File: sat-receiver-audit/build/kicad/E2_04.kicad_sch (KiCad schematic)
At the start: 54 parts, among them U214 TPS259630DDAR, U215 INA3221AIRGVR, U216 INA3221AIRGVR, U217 TLV3011BIDBVR, U218 TLV3011BIDBVR, U219 TLV3011BIDBVR, U220 TPS3701DDCR

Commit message: SR-RX-v2.1: review fixes on the Codex branch, readable schematic, one-file bundle
Independent review of the Codex branch (schematic vs STACK.md, hard rules,
security, tests) found no blockers; this commit applies its findings:

- rules in code: Cospas-Sarsat 406.0-406.1 MHz added to the no-data mask;
  Q6A Wi-Fi/BT off in the field/QUIET root (modprobe blacklist, udev
  authorized=0 on FE1.1s port 4, rfkill) with self-checks; device denylist
  completed per STACK (gr-gsm, gr-iridium, kalibrate, pager/trunking decoders,
  TX-capable tools); W1-2 WIFI_PWR_EN as blocking open item E5-10
- STACK.md is the source of truth again; v2.1 changes recorded in it; the
  "historical" marker kept only on ISDT/raw-balance rows; gender-neutral wording
- schematic data: open values shown as TBD with start values and notes, U503
  TPS2553DBVR-1, Lime X2/X4 RX mapping TBD, 37 open items drawn on the sheets
- schematic readability: wired groups, junctions, GND symbols, standard
  transistor/diode symbols; netlist unchanged (603 nets identical)
- tooling: reproducible run_checks (no timestamps or machine paths), pinned
  dependencies, bundle excludes cache folders, clean-checkout bundle check
- regenerated: KiCad export (14 pages), netlist/ERC, module lab, PCB inputs,
  readiness contract, acceptance hashes, SR-RX-v2-ves-proekt.html

Checks: ERC 0 errors/0 warnings, netlist comparison PASS, 432 tests (431
passed, 1 skipped), deployment tests OK, bundle check PASS on a clean checkout.

History note: earlier versions of the generated SR-RX-v2-ves-proekt.html and
handoff/handoff-bundle.zip were removed from history; only the final versions
are kept. The Codex merge commit is now attributed to Codex.

Co-Authored-By: Claude Opus 5.5 <noreply@anthropic.com>
Claude-Session: https://claude.ai/code/session_01W9CKpimWpgkUmrDQQMiKtF
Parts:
- removed C269: 100nF 50V X7R C1608X7R1H104K080AA, Capacitor_SMD:C_0603_1608Metric, symbol sr_rx_v2_completed:C_C269
- removed C270: 1uF 50V X7R C2012X7R1H105K125AB, Capacitor_SMD:C_0805_2012Metric, symbol sr_rx_v2_completed:C_C270
- removed C271: 1uF 50V X7R C2012X7R1H105K125AB, Capacitor_SMD:C_0805_2012Metric, symbol sr_rx_v2_completed:C_C271
- removed C272: 1uF 50V X7R C2012X7R1H105K125AB, Capacitor_SMD:C_0805_2012Metric, symbol sr_rx_v2_completed:C_C272
- removed C273: 47uF 50V EEUFR1H470, symbol sr_rx_v2_completed:C_C273
- removed C282: 10nF 50V C0G C1608C0G1H103J080AA, Capacitor_SMD:C_0603_1608Metric, symbol sr_rx_v2_completed:C_C282
- removed C283: 100nF 50V X7R C1608X7R1H104K080AA, Capacitor_SMD:C_0603_1608Metric, symbol sr_rx_v2_completed:C_C283
- removed C284: 10nF 50V C0G C1608C0G1H103J080AA, Capacitor_SMD:C_0603_1608Metric, symbol sr_rx_v2_completed:C_C284
- removed C285: 100nF 50V X7R C1608X7R1H104K080AA, Capacitor_SMD:C_0603_1608Metric, symbol sr_rx_v2_completed:C_C285
- removed C286: 10nF 50V C0G C1608C0G1H103J080AA, Capacitor_SMD:C_0603_1608Metric, symbol sr_rx_v2_completed:C_C286
- removed C287: 100nF 50V X7R C1608X7R1H104K080AA, Capacitor_SMD:C_0603_1608Metric, symbol sr_rx_v2_completed:C_C287
- removed C294: 22uF 50V X7R C3225X7R1H226M250AC, Capacitor_SMD:C_1210_3225Metric, symbol sr_rx_v2_completed:C_C294
- removed D203: PMEG4030ER, Diode_SMD:Nexperia_CFP3_SOD-123W, symbol sr_rx_v2_completed:C_D203
- removed L214: 1uH XAL5030-102MEC, symbol sr_rx_v2_completed:C_L214
- removed R262: 7.87k 1%, symbol sr_rx_v2_completed:C_R262
- removed R263: 112k 0.1%, symbol sr_rx_v2_completed:C_R263
- removed R264: 10.0k 0.1%, symbol sr_rx_v2_completed:C_R264
- removed R266: 0.200R 0.1% 0.25W Kelvin, symbol sr_rx_v2_completed:C_R266
- removed R267: 0.22R 1% 0.25W, symbol sr_rx_v2_completed:C_R267
- removed R280: 85.6k 0.1%, symbol sr_rx_v2_completed:C_R280
- removed R281: 10.0k 0.1%, symbol sr_rx_v2_completed:C_R281
- removed R283: 90.9k 0.1%, symbol sr_rx_v2_completed:C_R283
- removed R284: 10.0k 0.1%, symbol sr_rx_v2_completed:C_R284
- removed R286: 73.2k 0.1%, symbol sr_rx_v2_completed:C_R286
- removed R287: 10.0k 0.1%, symbol sr_rx_v2_completed:C_R287
- removed R288: TNPW0805332KBYEA 332k 0.1%10ppm, symbol sr_rx_v2_completed:C_R288
- removed TP212: BONI13V8, symbol sr_rx_v2_completed:C_TP212
- removed U214: TPS259630DDAR, symbol sr_rx_v2_completed:C_U214
- removed U217: TLV3011BIDBVR, symbol sr_rx_v2_completed:C_U217
- removed U218: TLV3011BIDBVR, symbol sr_rx_v2_completed:C_U218
- removed U219: TLV3011BIDBVR, symbol sr_rx_v2_completed:C_U219
- removed U220: TPS3701DDCR, symbol sr_rx_v2_completed:C_U220
- added C295: 1uF 50V X7R C2012X7R1H105K125AB, Capacitor_SMD:C_0805_2012Metric, symbol sr_rx_v2_completed:C_C295
- added C296: 1uF 50V X7R C2012X7R1H105K125AB, Capacitor_SMD:C_0805_2012Metric, symbol sr_rx_v2_completed:C_C296
- added C297: 1uF 50V X7R C2012X7R1H105K125AB, Capacitor_SMD:C_0805_2012Metric, symbol sr_rx_v2_completed:C_C297
- added C298: 47uF 50V EEUFR1H470, symbol sr_rx_v2_completed:C_C298
- added L215: 1uH XAL5030-102MEC, symbol sr_rx_v2_completed:C_L215
- added R293: 162k 1%, symbol sr_rx_v2_completed:C_R293
- added R294: 100k 1%, symbol sr_rx_v2_completed:C_R294
- added R295: 0.22R 1%0.25W, symbol sr_rx_v2_completed:C_R295
- added TP216: BIAS_SB_LNA, symbol sr_rx_v2_completed:C_TP216
- added U221: TPS2553DBVR-1, symbol sr_rx_v2_completed:C_U221
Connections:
- net GND: now also C295.2, C296.2, C297.2, C298.2 (-), R293.2, R294.2, U221.2 (GND)
- new net BIAS_SB_LNA: C297.1, L215.2, R295.1, TP216.1 (TP)
- new net E2_SB_DAMP: C298.1 (+), R295.2
- new net E2_SB_ILIM: R293.1, U221.5 (ILIM)
- new net E2_SB_SW: C296.1, L215.1, U221.6 (OUT)
- new net EN_SB_LNA: R294.1, U221.3 (EN)
- new net FLT_SB_LNA: U221.4 (FAULT)
- new net LAB5: C295.1, U221.1 (IN)
- no-connect marks 9 -> 8
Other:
- note added: "E2 - Захищені рейки, LNA і моніторинг струму (4/4)"
- note added: "S-band LaNA WB: захищена шина 5 V"
- note added: "Дроти з'єднують контакти всередині функціональної групи; кожне дерево дротів має одну глобальну мітку з канонічною назвою мережі (рамка-стрілка — мережа виходить за межі групи, пряма рамка — мережа лише цієї групи). Однакові мітки з'єднані на всіх аркушах; земля — символ GND. Рамки OPEN — незакриті ворота з design/E#.json (повний реєстр: OPEN_ITEMS.md); «TBD» у значенні — STACK номіналу не задає,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"
- note removed: "AUX12: контроль напруги після PTC"
- note removed: "Boni: контроль напруги"
- note removed: "Boni: малошумна захищена шина"
- note removed: "E2 - Захищені рейки, LNA і моніторинг струму (4/5)"
- note removed: "LNB: контроль напруги"
- note removed: "LNB: незалежне точне відсікання OVP"
- note removed: "Мережі з однаковими глобальними мітками електрично з'єднані на всіх аркушах. Фізичні/функціональні контакти: див. design/ і OPEN_ITEMS.md."
- title: E2 - Захищені рейки, LNA і моніторинг струму (4/5) -> E2 - Захищені рейки, LNA і моніторинг струму (4/4)
- moved on the sheet: U215, U216

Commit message: Stage 2 integration: CAD and DC_CORE re-freeze from CI run 40094234222; bound-count test and PCB hash lists follow
Co-Authored-By: Claude Opus 5.5 <noreply@anthropic.com>
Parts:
- removed C274: 100nF 50V X7R C1608X7R1H104K080AA, Capacitor_SMD:C_0603_1608Metric, symbol sr_rx_v2_completed:C_C274
- removed C275: 100nF 50V X7R C1608X7R1H104K080AA, Capacitor_SMD:C_0603_1608Metric, symbol sr_rx_v2_completed:C_C275
- removed C276: 100nF 50V X7R C1608X7R1H104K080AA, Capacitor_SMD:C_0603_1608Metric, symbol sr_rx_v2_completed:C_C276
- removed C277: 100nF 50V X7R C1608X7R1H104K080AA, Capacitor_SMD:C_0603_1608Metric, symbol sr_rx_v2_completed:C_C277
- removed C278: 100nF 50V X7R C1608X7R1H104K080AA, Capacitor_SMD:C_0603_1608Metric, symbol sr_rx_v2_completed:C_C278
- removed C279: 100nF 50V X7R C1608X7R1H104K080AA, Capacitor_SMD:C_0603_1608Metric, symbol sr_rx_v2_completed:C_C279
- removed C280: 100nF 50V X7R C1608X7R1H104K080AA, Capacitor_SMD:C_0603_1608Metric, symbol sr_rx_v2_completed:C_C280
- removed C281: 100nF 50V X7R C1608X7R1H104K080AA, Capacitor_SMD:C_0603_1608Metric, symbol sr_rx_v2_completed:C_C281
- removed C295: 1uF 50V X7R C2012X7R1H105K125AB, Capacitor_SMD:C_0805_2012Metric, symbol sr_rx_v2_completed:C_C295
- removed C296: 1uF 50V X7R C2012X7R1H105K125AB, Capacitor_SMD:C_0805_2012Metric, symbol sr_rx_v2_completed:C_C296
- removed C297: 1uF 50V X7R C2012X7R1H105K125AB, Capacitor_SMD:C_0805_2012Metric, symbol sr_rx_v2_completed:C_C297
- removed C298: 47uF 50V EEUFR1H470, symbol sr_rx_v2_completed:C_C298
- removed L215: 1uH XAL5030-102MEC, symbol sr_rx_v2_completed:C_L215
- removed R268: 10.0R 1%, symbol sr_rx_v2_completed:C_R268
- removed R269: 10.0R 1%, symbol sr_rx_v2_completed:C_R269
- removed R270: 10.0R 1%, symbol sr_rx_v2_completed:C_R270
- removed R271: 10.0R 1%, symbol sr_rx_v2_completed:C_R271
- removed R272: 10.0R 1%, symbol sr_rx_v2_completed:C_R272
- removed R273: 10.0R 1%, symbol sr_rx_v2_completed:C_R273
- removed R274: 10.0R 1%, symbol sr_rx_v2_completed:C_R274
- removed R275: 10.0R 1%, symbol sr_rx_v2_completed:C_R275
- removed R276: 10.0R 1%, symbol sr_rx_v2_completed:C_R276
- removed R277: 10.0R 1%, symbol sr_rx_v2_completed:C_R277
- removed R278: 10.0R 1%, symbol sr_rx_v2_completed:C_R278
- removed R279: 10.0R 1%, symbol sr_rx_v2_completed:C_R279
- removed R293: 162k 1%, symbol sr_rx_v2_completed:C_R293
- removed R294: 100k 1%, symbol sr_rx_v2_completed:C_R294
- removed R295: 0.22R 1%0.25W, symbol sr_rx_v2_completed:C_R295
- removed TP216: BIAS_SB_LNA, symbol sr_rx_v2_completed:C_TP216
- removed U215: INA3221AIRGVR, symbol sr_rx_v2_completed:C_U215
- removed U216: INA3221AIRGVR, symbol sr_rx_v2_completed:C_U216
- removed U221: TPS2553DBVR-1, symbol sr_rx_v2_completed:C_U221
- added C252: 10uF 50V X7R C3225X7R1H106K250AC, Capacitor_SMD:C_1210_3225Metric, symbol sr_rx_v2_completed:C_C252
- added C253: 10uF 50V X7R C3225X7R1H106K250AC, Capacitor_SMD:C_1210_3225Metric, symbol sr_rx_v2_completed:C_C253
- added C254: 47uF 50V EEUFR1H470, symbol sr_rx_v2_completed:C_C254
- added C255: 10uF 50V X7R C3225X7R1H106K250AC, Capacitor_SMD:C_1210_3225Metric, symbol sr_rx_v2_completed:C_C255
- added C256: 22uF 50V X7R C3225X7R1H226M250AC, Capacitor_SMD:C_1210_3225Metric, symbol sr_rx_v2_completed:C_C256
- added C257: 1uF 50V X7R C2012X7R1H105K125AB, Capacitor_SMD:C_0805_2012Metric, symbol sr_rx_v2_completed:C_C257
- added C258: 47nF 50V X7R C1608X7R1H473K080AA, Capacitor_SMD:C_0603_1608Metric, symbol sr_rx_v2_completed:C_C258
- added C259: 1uF 50V X7R C2012X7R1H105K125AB, Capacitor_SMD:C_0805_2012Metric, symbol sr_rx_v2_completed:C_C259
- added C260: 1uF 50V X7R C2012X7R1H105K125AB, Capacitor_SMD:C_0805_2012Metric, symbol sr_rx_v2_completed:C_C260
- added C261: 1uF 50V X7R C2012X7R1H105K125AB, Capacitor_SMD:C_0805_2012Metric, symbol sr_rx_v2_completed:C_C261
- added C262: 47uF 50V EEUFR1H470, symbol sr_rx_v2_completed:C_C262
- added C293: 22uF 50V X7R C3225X7R1H226M250AC, Capacitor_SMD:C_1210_3225Metric, symbol sr_rx_v2_completed:C_C293
- added D202: PMEG4030ER, Diode_SMD:Nexperia_CFP3_SOD-123W, symbol sr_rx_v2_completed:C_D202
- added L211: 1uH XAL5030-102MEC, symbol sr_rx_v2_completed:C_L211
- added L212: 1uH XAL5030-102MEC, symbol sr_rx_v2_completed:C_L212
- added R252: 0.22R 1% 0.25W, symbol sr_rx_v2_completed:C_R252
- added R253: 100k 1%, symbol sr_rx_v2_completed:C_R253
- added R254: 2.05k 1%, symbol sr_rx_v2_completed:C_R254
- added R255: 110k 0.5%, symbol sr_rx_v2_completed:C_R255
- added R256: 10.0k 0.5%, symbol sr_rx_v2_completed:C_R256
- added R258: 0.100R 0.1% 0.25W Kelvin, symbol sr_rx_v2_completed:C_R258
- added R259: 0.22R 1% 0.25W, symbol sr_rx_v2_completed:C_R259
- added TP211: LNB13V2, symbol sr_rx_v2_completed:C_TP211
- added U211: TPS7A4701RGWT, symbol sr_rx_v2_completed:C_U211
- added U212: TPS259630DDAR, symbol sr_rx_v2_completed:C_U212
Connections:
- net E2_LNB_EF: now also C259.1, R258.1, U212.5 (OUT)
- net E2_LNB_MON: now also C260.1, L212.1, R258.2
- net GND: now also C252.2, C253.2, C254.2 (-), C255.2, C256.2, C257.2, C258.2, C259.2, C260.2, C261.2, C262.2 (-), C293.2, D202.2 (A), R253.2, R254.2, R256.2, U211.10 (0P4V), U211.11 (0P2V), U211.5 (6P4V1), U211.6 (3P2V), U211.7 (GND), U211.8 (1P6V), U211.EP, U212.1 (GND), U212.EP
- new net E1_SW: C252.1, L211.1
- new net E2_LNB_DVDT: C258.1, U212.2 (dVdt)
- new net E2_LNB_ILM: R254.1, U212.7 (ILM)
- new net E2_LNB_IN: C253.1, C255.1, L211.2, R252.1, U211.15 (IN), U211.16 (IN)
- new net E2_LNB_IN_DAMP: C254.1 (+), R252.2
- new net E2_LNB_LDO: C256.1, C293.1, D202.1 (K), R255.1, U211.1 (OUT), U211.20 (OUT), U211.3 (SENSE/FB), U212.4 (IN)
- new net E2_LNB_NR: C257.1, U211.14 (NR)
- new net E2_LNB_OV: R255.2, R256.1, U212.8 (OVLO)
- new net EN_LNB: R253.1, U211.13 (EN)
- new net FLT_LNB: U212.6 (FLT)
- new net LNB13V2: C261.1, L212.2, R259.1, TP211.1 (TP)
- new net LNB13V2_DAMP: C262.1 (+), R259.2
- new net OVP_LNB_N: U212.3 (EN/UVLO)
- no-connect marks 8 -> 7
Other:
- note added: "E2 - Захищені рейки, LNA і моніторинг струму (4/5)"
- note added: "E2-02 — OPEN, блокує випуск — STACK §5.1 (LNB13V2); §8 (TPS7A4701); §8.1 RF-4"
- note added: "LNB: малошумна захищена шина"
- note added: "Позначення фізичних джерел живлення (ERC)"
- note added: "Статичне вікно OVP LNB закрито TPS3701: 13.56–13.96V. Швидкий викид при відмові LDO не обмежено гарантованим максимальним часом у даташитах: 9.9µs компаратора і близько 12µs EN-off eFuse задані лише типово. Ворота (стенд): Без LNB і зі струмовим обмеженням подати на вузол LDO контрольований стрибок 13.2→16.4V; осцилографувати F-вихід при мін./макс. навантаженні, на холоді й при 50°C. Отримати гра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"
- note removed: "E2 - Захищені рейки, LNA і моніторинг струму (4/4)"
- note removed: "INA3221: струми LNA1–3"
- note removed: "INA3221: струми LNA4, LNB і Boni"
- note removed: "S-band LaNA WB: захищена шина 5 V"
- title: E2 - Захищені рейки, LNA і моніторинг струму (4/4) -> E2 - Захищені рейки, LNA і моніторинг струму (4/5)

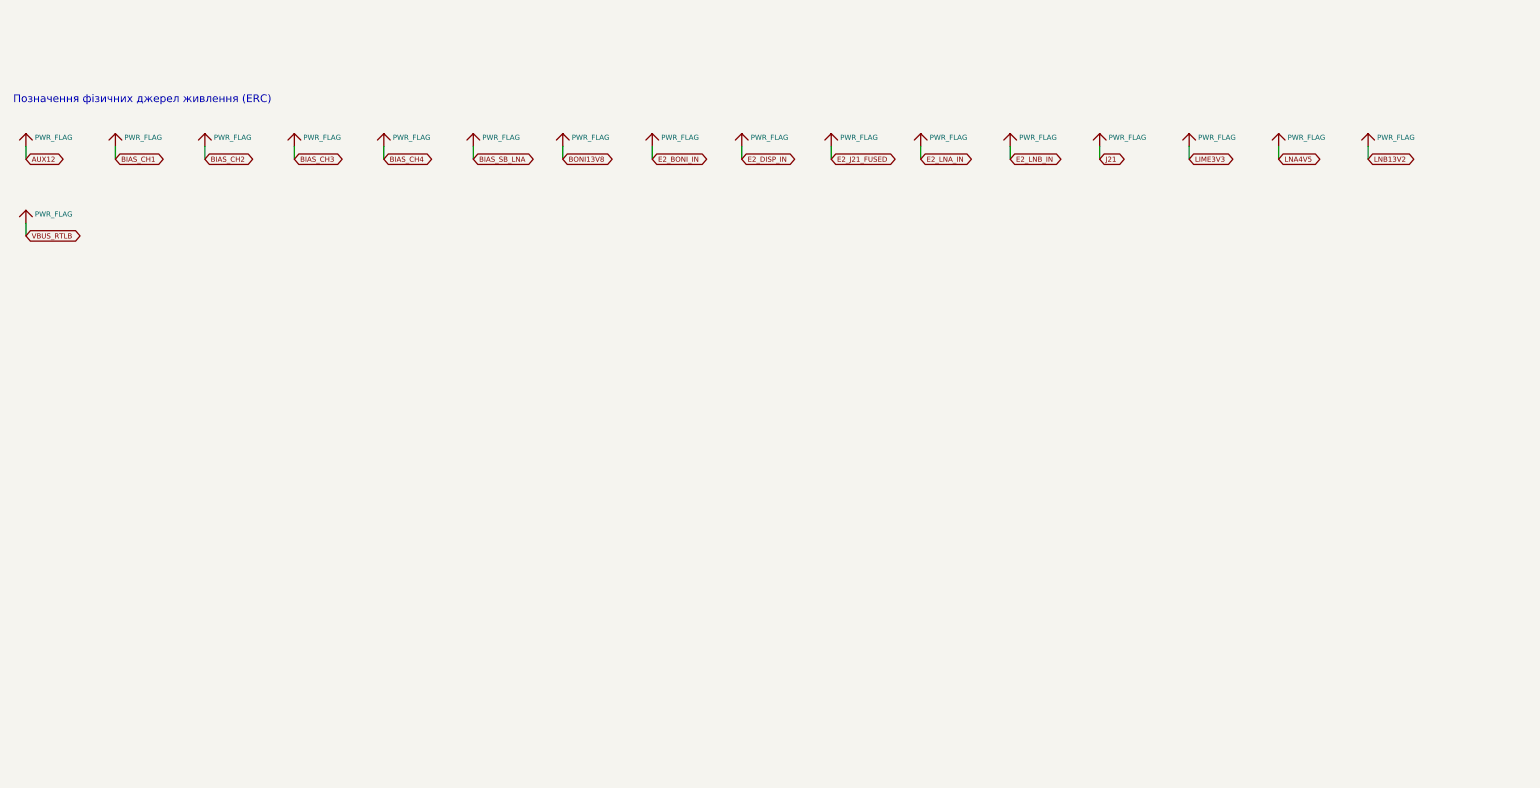
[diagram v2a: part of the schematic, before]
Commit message: GENERATED: CAD, documents, verification reports, DC_CORE re-freeze and module-lab inventory for f3f57e8
Applied unchanged from the cad-regenerated artifact of CI run 40109759054
(workflow_dispatch, refreeze_pcb=true, KiCad 10.0.7): schematics, SVG, PDF,
netlist, OPEN_ITEMS.md, COMPLETION.md, verification/{electrical-invariants,
independent-netlist-review,netlist,pcb-review,pcb-prototype-review,
pdf-export,validation}, pcb/generated and the re-frozen DC_CORE starter and
routed prototype with their pinned hashes. Inputs: the stage 3A merge,
design/E2.json (PICO-2 text) and STACK.md (2.7 row).

deployment/module_lab/inventory.json: source_snapshots only, from
deployment/module_lab/refresh_inventory.py (E2.json and STACK.md bytes).

Co-Authored-By: Claude Opus 5.5 <noreply@anthropic.com>
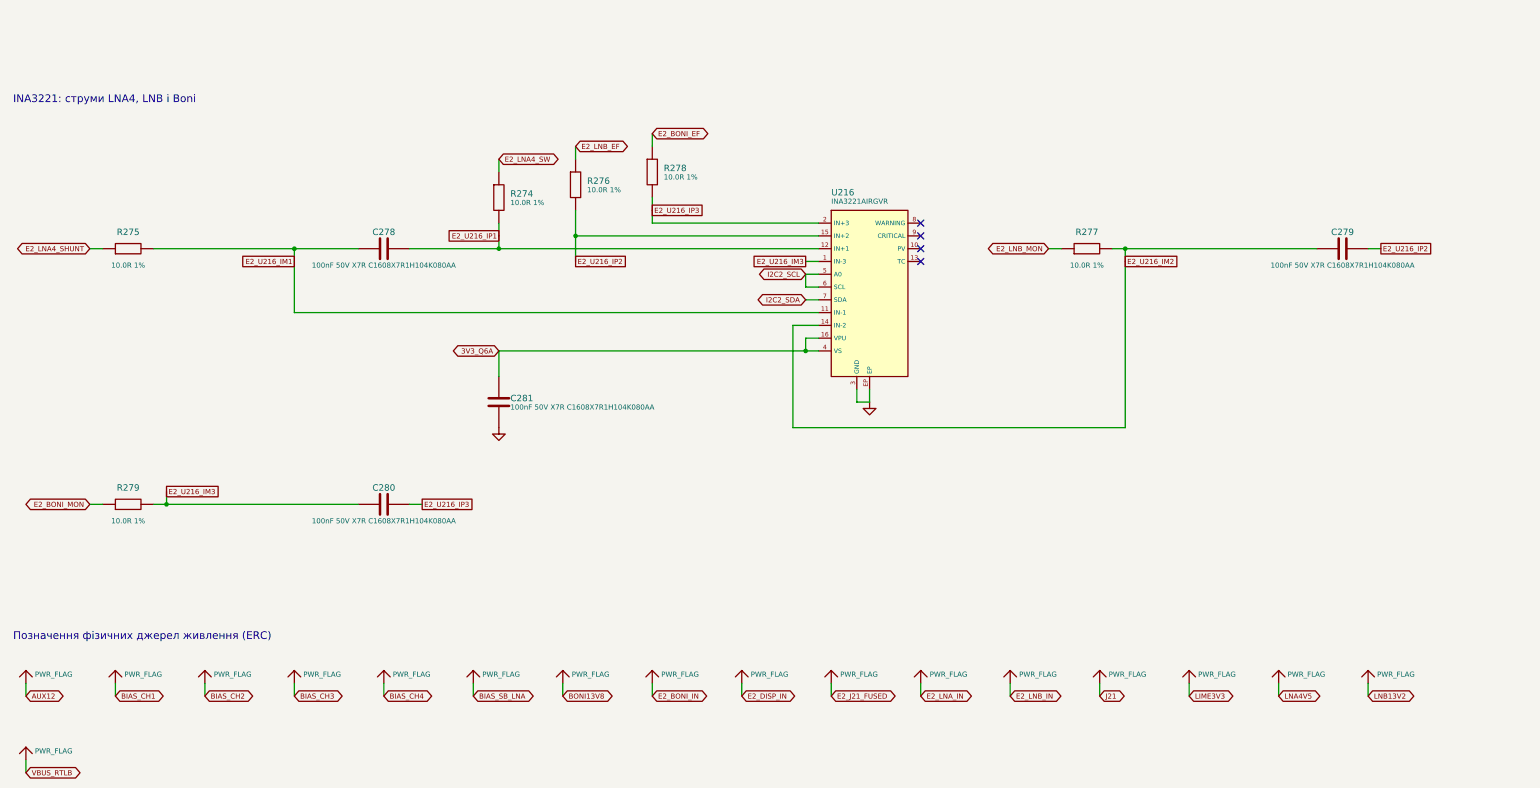
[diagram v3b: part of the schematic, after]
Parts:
- added C278: 100nF 50V X7R C1608X7R1H104K080AA, Capacitor_SMD:C_0603_1608Metric, symbol sr_rx_v2_completed:C_C278
- added C279: 100nF 50V X7R C1608X7R1H104K080AA, Capacitor_SMD:C_0603_1608Metric, symbol sr_rx_v2_completed:C_C279
- added C280: 100nF 50V X7R C1608X7R1H104K080AA, Capacitor_SMD:C_0603_1608Metric, symbol sr_rx_v2_completed:C_C280
- added C281: 100nF 50V X7R C1608X7R1H104K080AA, Capacitor_SMD:C_0603_1608Metric, symbol sr_rx_v2_completed:C_C281
- added R274: 10.0R 1%, symbol sr_rx_v2_completed:C_R274
- added R275: 10.0R 1%, symbol sr_rx_v2_completed:C_R275
- added R276: 10.0R 1%, symbol sr_rx_v2_completed:C_R276
- added R277: 10.0R 1%, symbol sr_rx_v2_completed:C_R277
- added R278: 10.0R 1%, symbol sr_rx_v2_completed:C_R278
- added R279: 10.0R 1%, symbol sr_rx_v2_completed:C_R279
- added U216: INA3221AIRGVR, symbol sr_rx_v2_completed:C_U216
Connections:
- net E2_LNB_EF: now also R276.1
- net E2_LNB_MON: now also R277.1
- net GND: now also C281.2, U216.3 (GND), U216.EP
- new net 3V3_Q6A: C281.1, U216.16 (VPU), U216.4 (VS)
- new net E2_BONI_EF: R278.1
- new net E2_BONI_MON: R279.1
- new net E2_LNA4_SHUNT: R275.1
- new net E2_LNA4_SW: R274.1
- new net E2_U216_IM1: C278.2, R275.2, U216.11 (IN-1)
- new net E2_U216_IM2: C279.2, R277.2, U216.14 (IN-2)
- new net E2_U216_IM3: C280.2, R279.2, U216.1 (IN-3)
- new net E2_U216_IP1: C278.1, R274.2, U216.12 (IN+1)
- new net E2_U216_IP2: C279.1, R276.2, U216.15 (IN+2)
- new net E2_U216_IP3: C280.1, R278.2, U216.2 (IN+3)
- new net I2C2_SCL: U216.5 (A0), U216.6 (SCL)
- new net I2C2_SDA: U216.7 (SDA)
- no-connect marks 7 -> 11
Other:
- note added: "INA3221: струми LNA4, LNB і Boni"
